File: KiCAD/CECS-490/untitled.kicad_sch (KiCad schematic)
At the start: 5 parts, among them U10 74HC595, U12 74HC595, U4 74HC595, U5 74HC595, U8 74HC595

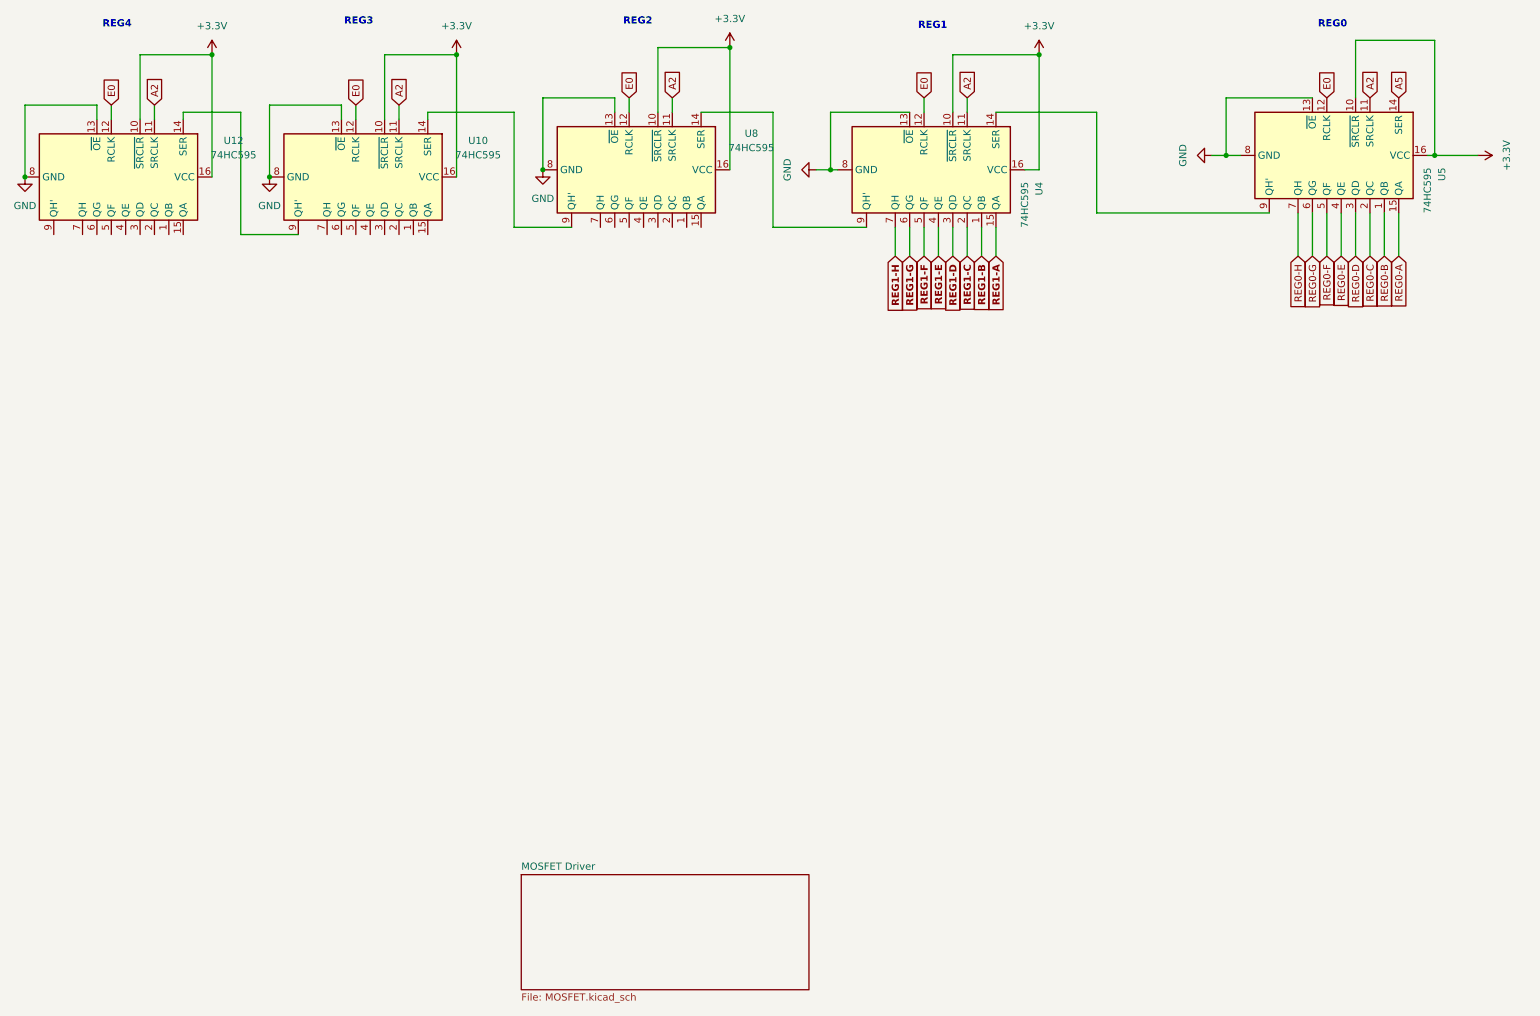
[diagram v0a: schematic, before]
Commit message: Added support circuit for MCU
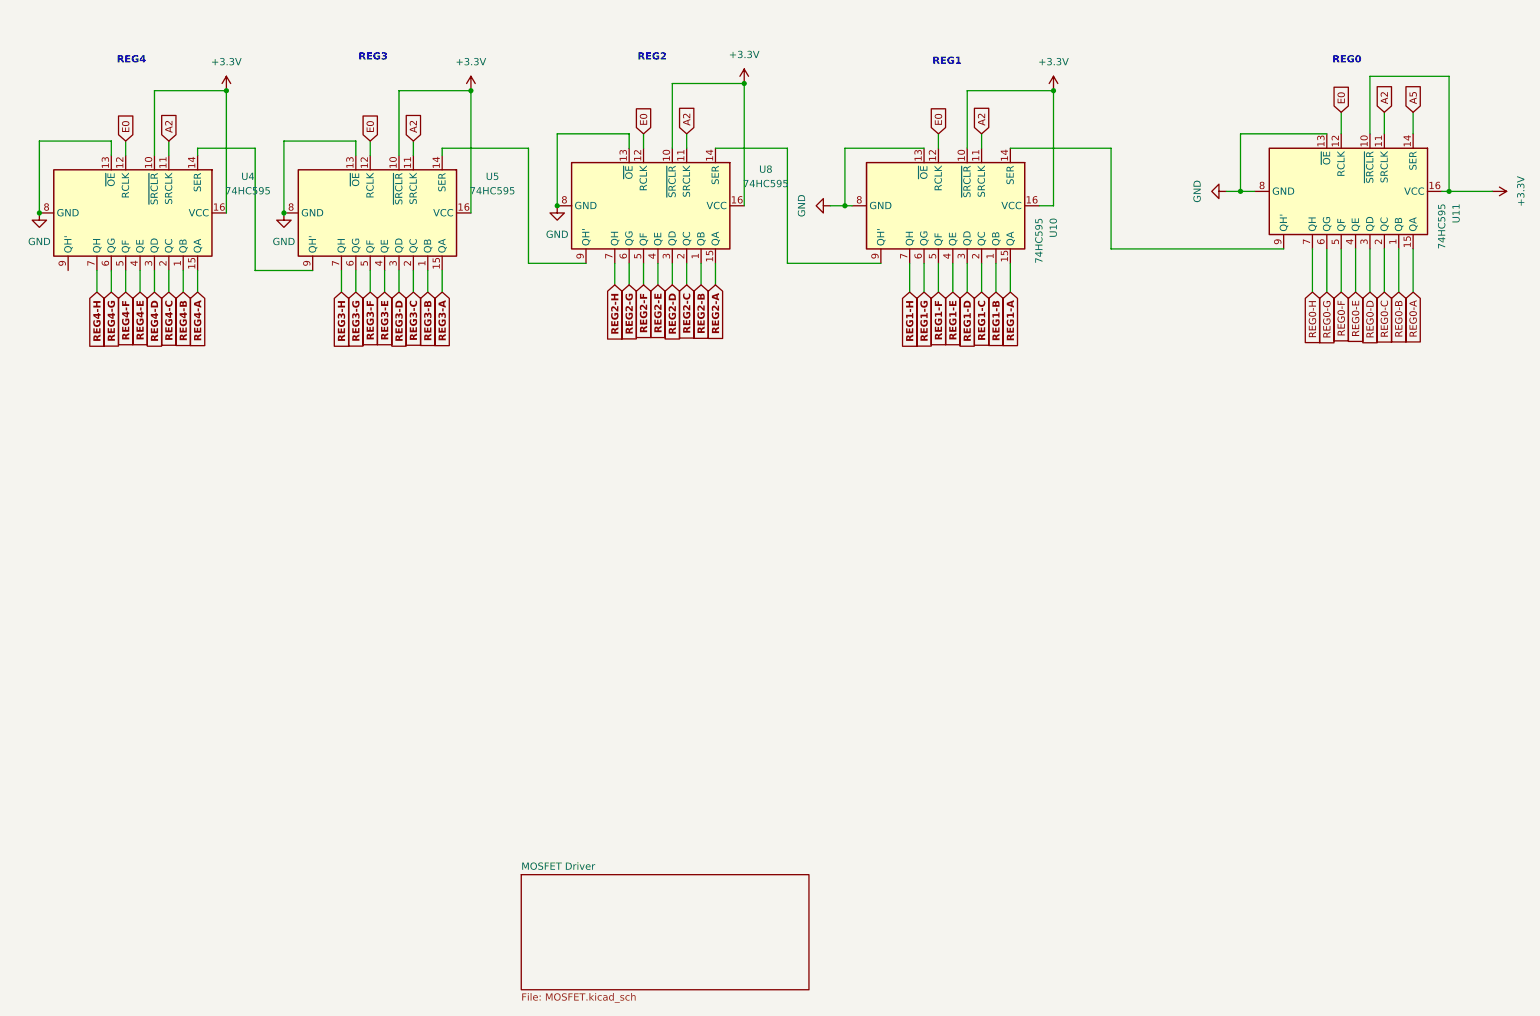
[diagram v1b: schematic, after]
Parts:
- removed U12: 74HC595, symbol 74xx:74HC595
- added U11: 74HC595, symbol 74xx:74HC595
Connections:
- net +3.3V: now also U11.10 (~{SRCLR}), U11.16 (VCC)
- net A2: now also U11.11 (SRCLK)
- net A5: now also U11.14 (SER); no longer U5.14 (SER)
- net E0: now also U11.12 (RCLK)
- net GND: now also U11.13 (~{OE}), U11.8 (GND)
- net REG0-A: now also U11.15 (QA); no longer U5.15 (QA)
- net REG0-B: now also U11.1 (QB); no longer U5.1 (QB)
- net REG0-C: now also U11.2 (QC); no longer U5.2 (QC)
- net REG0-D: now also U11.3 (QD); no longer U5.3 (QD)
- net REG0-E: now also U11.4 (QE); no longer U5.4 (QE)
- net REG0-F: now also U11.5 (QF); no longer U5.5 (QF)
- net REG0-G: now also U11.6 (QG); no longer U5.6 (QG)
- net REG0-H: now also U11.7 (QH); no longer U5.7 (QH)
- net REG1-A: now also U10.15 (QA); no longer U4.15 (QA)
- net REG1-B: now also U10.1 (QB); no longer U4.1 (QB)
- net REG1-C: now also U10.2 (QC); no longer U4.2 (QC)
- net REG1-D: now also U10.3 (QD); no longer U4.3 (QD)
- net REG1-E: now also U10.4 (QE); no longer U4.4 (QE)
- net REG1-F: now also U10.5 (QF); no longer U4.5 (QF)
- net REG1-G: now also U10.6 (QG); no longer U4.6 (QG)
- net REG1-H: now also U10.7 (QH); no longer U4.7 (QH)
- net at U10.14 (SER): now also U11.9 (QH'); no longer U8.9 (QH')
- net at U10.9 (QH'): now also U8.14 (SER)
- net REG2-B: now reaches U8.1 (QB)
- net at U4.9 (QH'): no longer U8.14 (SER)
- net REG2-A: now reaches U8.15 (QA)
- net REG2-C: now reaches U8.2 (QC)
- net REG2-D: now reaches U8.3 (QD)
- net REG2-E: now reaches U8.4 (QE)
- net REG2-F: now reaches U8.5 (QF)
- net REG2-G: now reaches U8.6 (QG)
- net REG2-H: now reaches U8.7 (QH)
- new net: U5.14 (SER), U8.9 (QH')
- new net REG3-A: U5.15 (QA)
- new net REG3-B: U5.1 (QB)
- new net REG3-C: U5.2 (QC)
- new net REG3-D: U5.3 (QD)
- new net REG3-E: U5.4 (QE)
- new net REG3-F: U5.5 (QF)
- new net REG3-G: U5.6 (QG)
- new net REG3-H: U5.7 (QH)
- new net REG4-A: U4.15 (QA)
- new net REG4-B: U4.1 (QB)
- new net REG4-C: U4.2 (QC)
- new net REG4-D: U4.3 (QD)
- new net REG4-E: U4.4 (QE)
- new net REG4-F: U4.5 (QF)
- new net REG4-G: U4.6 (QG)
- new net REG4-H: U4.7 (QH)
